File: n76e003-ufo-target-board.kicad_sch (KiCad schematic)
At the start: 12 parts, among them J1 CW308T_CONNBOARD, J4 Conn_01x02_Pin, U2 N76E003AT20

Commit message: Remove C2, add url to board
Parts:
- removed C2: 2.2uF, Capacitor_SMD:C_0805_2012Metric_Pad1.18x1.45mm_HandSolder, symbol Device:C_Small
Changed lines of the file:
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@@
   (junction (at 92.71 137.795) (diameter 0) (color 0 0 0 0)
   )
-  (junction (at 213.36 111.125) (diameter 0) (color 0 0 0 0)
-  )
   (junction (at 94.615 130.175) (diameter 0) (color 0 0 0 0)
   )
@@
   )
   (junction (at 193.04 117.475) (diameter 0) (color 0 0 0 0)
-  )
-  (junction (at 213.36 104.775) (diameter 0) (color 0 0 0 0)
   )
   (no_connect (at 121.285 155.575))
@@
   (no_connect (at 179.705 107.315))
   (no_connect (at 126.365 155.575))
+  (bus_entry (at -22.86 66.04) (size 2.54 2.54)
+    (stroke (width 0) (type default))
+  )
   (wire (pts (xy 53.34 108.585) (xy 53.34 117.475))
     (stroke (width 0) (type default))
@@
     (stroke (width 0) (type default))
   )
-  (wire (pts (xy 213.36 104.775) (xy 224.79 104.775))
-    (stroke (width 0) (type default))
-  )
   (wire (pts (xy 154.305 165.735) (xy 90.805 165.735))
     (stroke (width 0) (type default))
@@
     (stroke (width 0) (type default))
   )
-  (wire (pts (xy 224.79 111.125) (xy 224.79 109.855))
-    (stroke (width 0) (type default))
-  )
   (wire (pts (xy 78.74 137.795) (xy 92.71 137.795))
     (stroke (width 0) (type default))
@@
     (stroke (width 0) (type default))
   )
-  (wire (pts (xy 213.36 111.125) (xy 213.36 109.855))
+  (wire (pts (xy 213.36 109.855) (xy 213.36 113.03))
     (stroke (width 0) (type default))
   )
@@
     (stroke (width 0) (type default))
   )
-  (wire (pts (xy 213.36 113.03) (xy 213.36 111.125))
-    (stroke (width 0) (type default))
-  )
   (wire (pts (xy 154.305 155.575) (xy 154.305 165.735))
     (stroke (width 0) (type default))
@@
   )
   (wire (pts (xy 80.645 112.395) (xy 86.995 112.395))
-    (stroke (width 0) (type default))
-  )
-  (wire (pts (xy 213.36 111.125) (xy 224.79 111.125))
     (stroke (width 0) (type default))
   )
@@
         )
       )
-    )
-  )
-  (symbol (lib_id "Device:C_Small") (at 224.79 107.315 0) (unit 1)
-    (in_bom yes) (on_board yes) (dnp no) (fields_autoplaced)
-    (property "Reference" "C2" (at 227.33 106.6863 0)
-      (effects (font (size 1.27 1.27)) (justify left))
-    )
-    (property "Value" "2.2uF" (at 227.33 109.2263 0)
-      (effects (font (size 1.27 1.27)) (justify left))
-    )
-    (property "Footprint" "Capacitor_SMD:C_0805_2012Metric_Pad1.18x1.45mm_HandSolder" (at 224.79 107.315 0)
-      (effects (font (size 1.27 1.27)) hide)
-    )
-    (property "Datasheet" "~" (at 224.79 107.315 0)
-      (effects (font (size 1.27 1.27)) hide)
-    )
-    (pin "1")
-    (pin "2")
-    (instances
-      (project "n76e003-ufo-target-board"
-        (path "/e139b73c-4b3b-4226-b99b-9f4c47aa4c67"
-          (reference "C2") (unit 1)
-        )
-      )

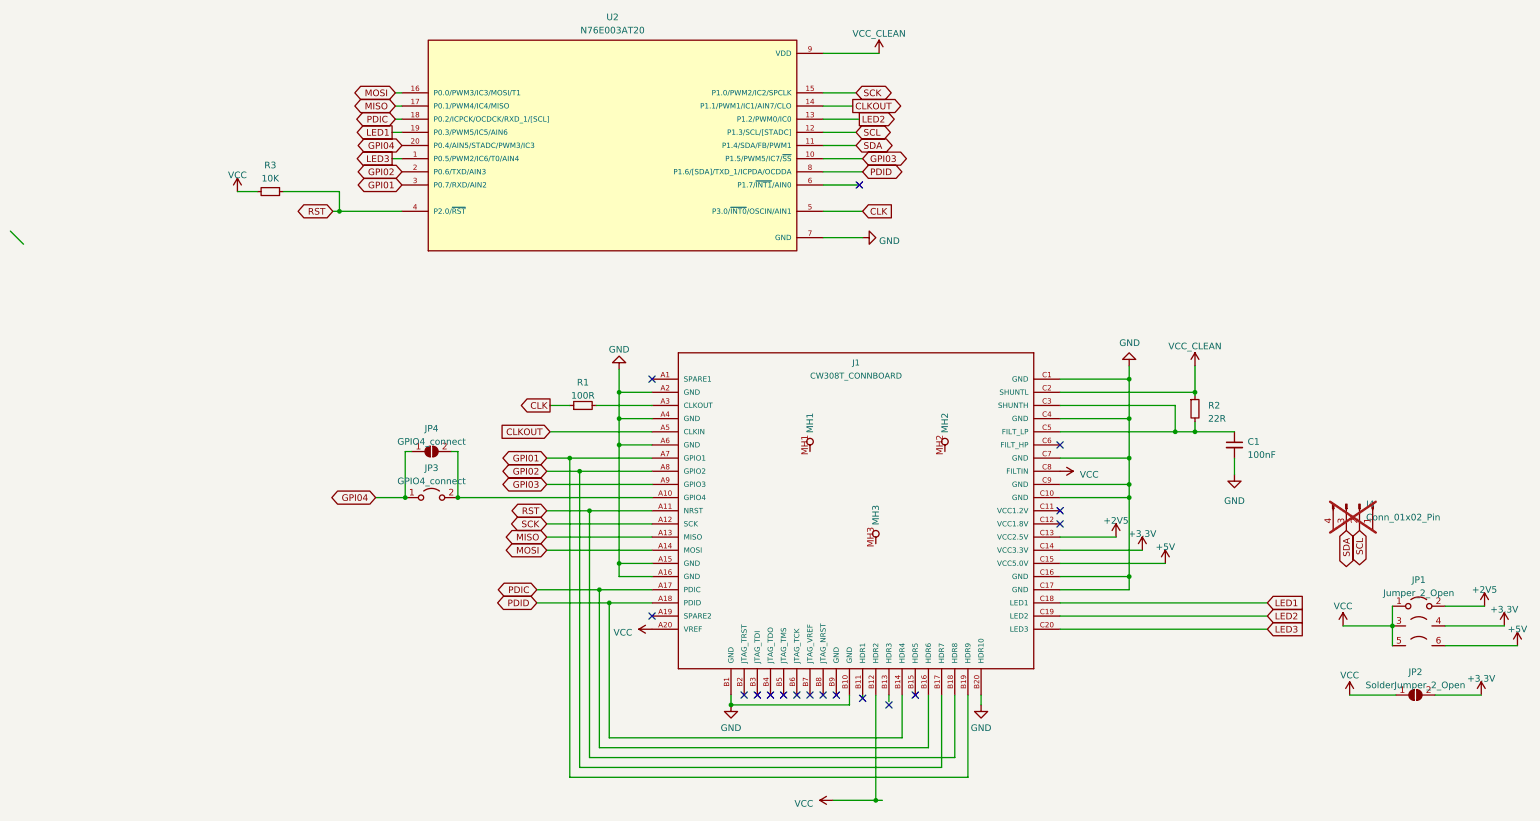
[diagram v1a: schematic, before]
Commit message: switch gpio1 and gpio2 lines, update gerbers, notes
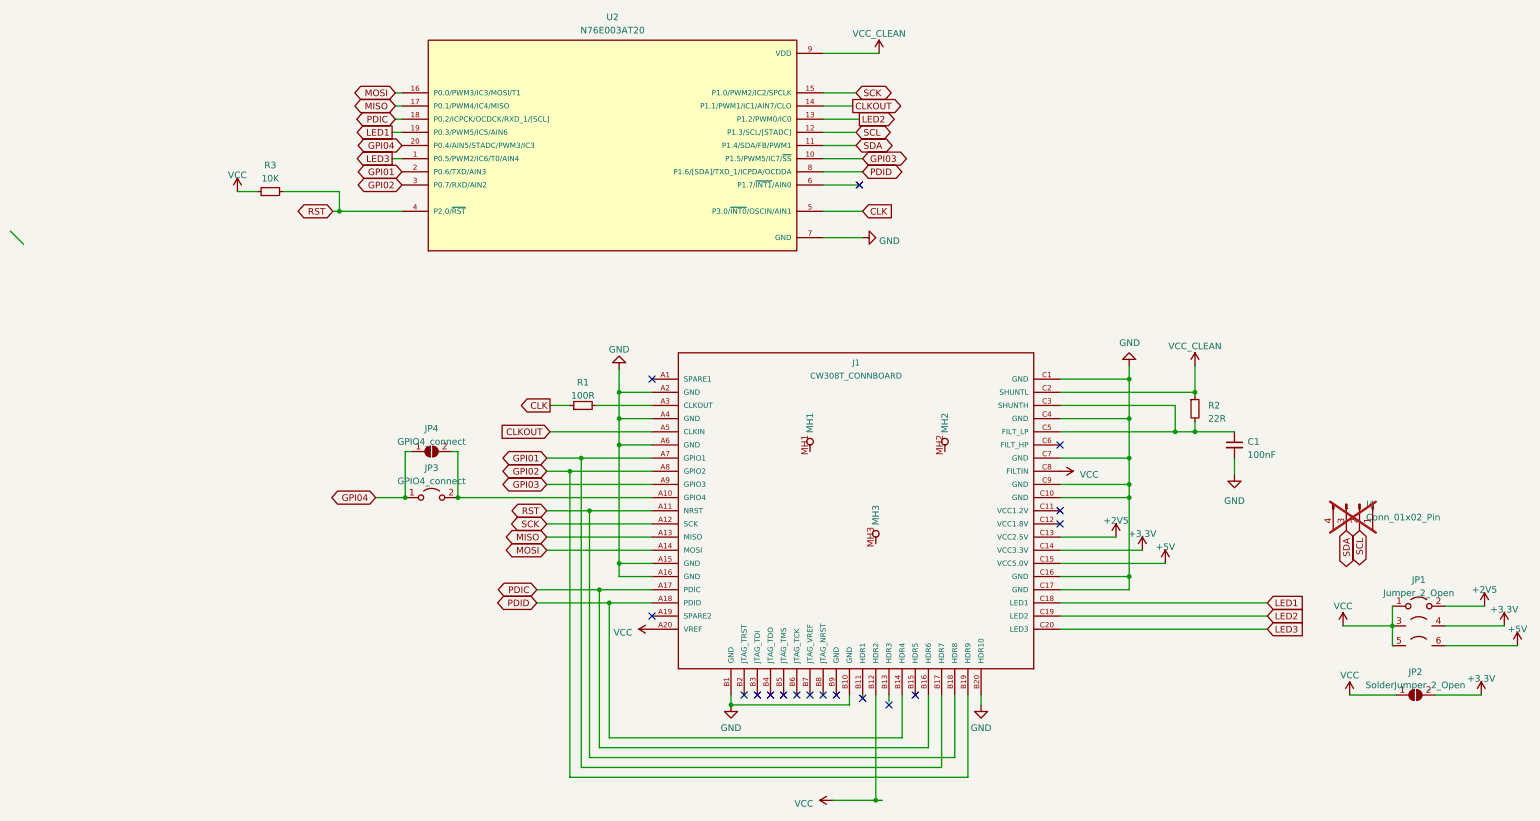
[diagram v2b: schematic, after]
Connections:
- net GPI01: now also J1.B17 (HDR7), U2.2 (P0.6/TXD/AIN3); no longer J1.B19 (HDR9), U2.3 (P0.7/RXD/AIN2)
- net GPI02: now also J1.B19 (HDR9), U2.3 (P0.7/RXD/AIN2); no longer J1.B17 (HDR7), U2.2 (P0.6/TXD/AIN3)
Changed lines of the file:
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@@
   (junction (at 205.74 97.155) (diameter 0) (color 0 0 0 0)
   )
-  (junction (at 86.995 112.395) (diameter 0) (color 0 0 0 0)
-  )
   (junction (at 243.84 142.24) (diameter 0) (color 0 0 0 0)
   )
@@
   (junction (at 116.205 157.48) (diameter 0) (color 0 0 0 0)
   )
-  (junction (at 85.09 109.855) (diameter 0) (color 0 0 0 0)
-  )
   (junction (at 88.9 120.015) (diameter 0) (color 0 0 0 0)
   )
@@
   (junction (at 201.93 104.775) (diameter 0) (color 0 0 0 0)
   )
+  (junction (at 85.1215 112.395) (diameter 0) (color 0 0 0 0)
+  )
   (junction (at 94.615 107.315) (diameter 0) (color 0 0 0 0)
+  )
+  (junction (at 87.3052 109.855) (diameter 0) (color 0 0 0 0)
   )
   (junction (at 53.34 117.475) (diameter 0) (color 0 0 0 0)
@@
     (stroke (width 0) (type default))
   )
-  (wire (pts (xy 86.995 169.545) (xy 86.995 112.395))
+  (wire (pts (xy 87.3052 169.5503) (xy 87.3052 109.855))
     (stroke (width 0) (type default))
   )
@@
     (stroke (width 0) (type default))
   )
-  (wire (pts (xy 85.09 109.855) (xy 100.965 109.855))
+  (wire (pts (xy 80.645 109.855) (xy 87.3052 109.855))
     (stroke (width 0) (type default))
   )
@@
     (stroke (width 0) (type default))
   )
-  (wire (pts (xy 85.09 171.45) (xy 85.09 109.855))
+  (wire (pts (xy 85.1215 171.45) (xy 85.1215 112.395))
     (stroke (width 0) (type default))
   )
@@
     (stroke (width 0) (type default))
   )
-  (wire (pts (xy 86.995 112.395) (xy 100.965 112.395))
+  (wire (pts (xy 85.1215 112.395) (xy 100.965 112.395))
     (stroke (width 0) (type default))
   )
@@
     (stroke (width 0) (type default))
   )
-  (wire (pts (xy 156.845 155.575) (xy 156.845 169.545))
+  (wire (pts (xy 87.3052 109.855) (xy 100.965 109.855))
+    (stroke (width 0) (type default))
+  )
+  (wire (pts (xy 156.845 155.575) (xy 156.845 169.5503))
     (stroke (width 0) (type default))
   )
@@
     (stroke (width 0) (type default))
   )
-  (wire (pts (xy 80.645 109.855) (xy 85.09 109.855))
-    (stroke (width 0) (type default))
-  )
   (wire (pts (xy 53.34 108.585) (xy 54.61 108.585))
     (stroke (width 0) (type default))
   )
-  (wire (pts (xy 80.645 112.395) (xy 86.995 112.395))
+  (wire (pts (xy 80.645 112.395) (xy 85.1215 112.395))
     (stroke (width 0) (type default))
   )
@@
     (stroke (width 0) (type default))
   )
-  (wire (pts (xy 156.845 169.545) (xy 86.995 169.545))
+  (wire (pts (xy 156.845 169.5503) (xy 87.3052 169.5503))
     (stroke (width 0) (type default))
   )
@@
     (stroke (width 0) (type default))
   )
-  (wire (pts (xy 161.925 171.45) (xy 85.09 171.45))
+  (wire (pts (xy 161.925 171.45) (xy 85.1215 171.45))
     (stroke (width 0) (type default))
   )
@@
     )
   )
+  (global_label "GPI01" (shape bidirectional) (at 52.705 54.61 180) (fields_autoplaced)
+    (effects (font (size 1.27 1.27)) (justify right))
+    (property "Intersheetrefs" "${INTERSHEET_REFS}" (at 43.1241 54.61 0)
+      (effects (font (size 1.27 1.27)) (justify right) hide)
+    )
+  )
   (global_label "CLKOUT" (shape output) (at 139.7 41.91 0) (fields_autoplaced)
     (effects (font (size 1.27 1.27)) (justify left))
@@
     )
   )
-  (global_label "GPI01" (shape bidirectional) (at 52.705 57.15 180) (fields_autoplaced)
+  (global_label "PDIC" (shape bidirectional) (at 78.74 135.255 180) (fields_autoplaced)
+    (effects (font (size 1.27 1.27)) (justify right))
+    (property "Intersheetrefs" "${INTERSHEET_REFS}" (at 70.3081 135.255 0)
+      (effects (font (size 1.27 1.27)) (justify right) hide)
+    )
+  )
+  (global_label "SDA" (shape bidirectional) (at 140.335 49.53 0) (fields_autoplaced)
+    (effects (font (size 1.27 1.27)) (justify left))
+    (property "Intersheetrefs" "${INTERSHEET_REFS}" (at 147.9202 49.53 0)
+      (effects (font (size 1.27 1.27)) (justify left) hide)
+    )
+  )
+  (global_label "SCL" (shape bidirectional) (at 237.49 123.825 270) (fields_autoplaced)
+    (effects (font (size 1.27 1.27)) (justify right))
+    (property "Intersheetrefs" "${INTERSHEET_REFS}" (at 237.49 131.3497 90)
+      (effects (font (size 1.27 1.27)) (justify right) hide)
+    )
+  )
+  (global_label "PDIC" (shape bidirectional) (at 51.435 44.45 180) (fields_autoplaced)
+    (effects (font (size 1.27 1.27)) (justify right))
+    (property "Intersheetrefs" "${INTERSHEET_REFS}" (at 43.0031 44.45 0)
+      (effects (font (size 1.27 1.27)) (justify right) hide)
+    )
+  )
+  (global_label "GPI04" (shape bidirectional) (at 47.625 117.475 180) (fields_autoplaced)
+    (effects (font (size 1.27 1.27)) (justify right))
+    (property "Intersheetrefs" "${INTERSHEET_REFS}" (at 38.0441 117.475 0)
+      (effects (font (size 1.27 1.27)) (justify right) hide)
+    )
+  )
+  (global_label "LED3" (shape output) (at 50.8 52.07 180) (fields_autoplaced)
+    (effects (font (size 1.27 1.27)) (justify right))
+    (property "Intersheetrefs" "${INTERSHEET_REFS}" (at 43.2376 52.07 0)
+      (effects (font (size 1.27 1.27)) (justify right) hide)
+    )
+  )
+  (global_label "MOSI" (shape bidirectional) (at 80.645 127.635 180) (fields_autoplaced)
+    (effects (font (size 1.27 1.27)) (justify right))
+    (property "Intersheetrefs" "${INTERSHEET_REFS}" (at 72.0317 127.635 0)
+      (effects (font (size 1.27 1.27)) (justify right) hide)
+    )
+  )
+  (global_label "RST" (shape bidirectional) (at 80.645 120.015 180) (fields_autoplaced)
+    (effects (font (size 1.27 1.27)) (justify right))
+    (property "Intersheetrefs" "${INTERSHEET_REFS}" (at 73.1808 120.015 0)
+      (effects (font (size 1.27 1.27)) (justify right) hide)
+    )
+  )
+  (global_label "GPI02" (shape bidirectional) (at 52.705 57.15 180) (fields_autoplaced)
     (effects (font (size 1.27 1.27)) (justify right))
     (property "Intersheetrefs" "${INTERSHEET_REFS}" (at 43.1241 57.15 0)
@@
     )
   )
-  (global_label "PDIC" (shape bidirectional) (at 78.74 135.255 180) (fields_autoplaced)
-    (effects (font (size 1.27 1.27)) (justify right))
-    (property "Intersheetrefs" "${INTERSHEET_REFS}" (at 70.3081 135.255 0)
-      (effects (font (size 1.27 1.27)) (justify right) hide)
-    )
-  )
-  (global_label "SDA" (shape bidirectional) (at 140.335 49.53 0) (fields_autoplaced)
-    (effects (font (size 1.27 1.27)) (justify left))
-    (property "Intersheetrefs" "${INTERSHEET_REFS}" (at 147.9202 49.53 0)
-      (effects (font (size 1.27 1.27)) (justify left) hide)
-    )
-  )
-  (global_label "SCL" (shape bidirectional) (at 237.49 123.825 270) (fields_autoplaced)
-    (effects (font (size 1.27 1.27)) (justify right))
-    (property "Intersheetrefs" "${INTERSHEET_REFS}" (at 237.49 131.3497 90)
-      (effects (font (size 1.27 1.27)) (justify right) hide)
-    )
-  )
-  (global_label "PDIC" (shape bidirectional) (at 51.435 44.45 180) (fields_autoplaced)
-    (effects (font (size 1.27 1.27)) (justify right))
-    (property "Intersheetrefs" "${INTERSHEET_REFS}" (at 43.0031 44.45 0)
-      (effects (font (size 1.27 1.27)) (justify right) hide)
-    )
-  )
-  (global_label "GPI04" (shape bidirectional) (at 47.625 117.475 180) (fields_autoplaced)
-    (effects (font (size 1.27 1.27)) (justify right))
-    (property "Intersheetrefs" "${INTERSHEET_REFS}" (at 38.0441 117.475 0)
-      (effects (font (size 1.27 1.27)) (justify right) hide)
-    )
-  )
-  (global_label "LED3" (shape output) (at 50.8 52.07 180) (fields_autoplaced)
-    (effects (font (size 1.27 1.27)) (justify right))
-    (property "Intersheetrefs" "${INTERSHEET_REFS}" (at 43.2376 52.07 0)
-      (effects (font (size 1.27 1.27)) (justify right) hide)
-    )
-  )
-  (global_label "MOSI" (shape bidirectional) (at 80.645 127.635 180) (fields_autoplaced)
-    (effects (font (size 1.27 1.27)) (justify right))
-    (property "Intersheetrefs" "${INTERSHEET_REFS}" (at 72.0317 127.635 0)
-      (effects (font (size 1.27 1.27)) (justify right) hide)
-    )
-  )
-  (global_label "RST" (shape bidirectional) (at 80.645 120.015 180) (fields_autoplaced)
-    (effects (font (size 1.27 1.27)) (justify right))
-    (property "Intersheetrefs" "${INTERSHEET_REFS}" (at 73.1808 120.015 0)
-      (effects (font (size 1.27 1.27)) (justify right) hide)
-    )
-  )
   (global_label "LED2" (shape input) (at 219.71 140.335 0) (fields_autoplaced)
     (effects (font (size 1.27 1.27)) (justify left))
@@
       (effects (font (size 1.27 1.27)) (justify right) hide)
     )
-  )
-  (global_label "GPI02" (shape bidirectional) (at 52.705 54.61 180) (fields_autoplaced)
-    (effects (font (size 1.27 1.27)) (justify right))
-    (property "Intersheetrefs" "${INTERSHEET_REFS}" (at 43.1241 54.61 0)
-      (effects (font (size 1.27 1.27)) (justify right) hide)
-    )

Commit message: add C2 footprint back, exclude from BOM by default
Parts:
- added C2: 2.2uF (OPT), Capacitor_SMD:C_0805_2012Metric_Pad1.18x1.45mm_HandSolder, symbol Device:C_Small
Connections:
- net GND: now also C2.2
- net at C1.1, J1.C3 (SHUNTH), J1.C5 (FILT_LP)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: now also C2.1
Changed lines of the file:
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@@
 (kicad_sch (version 20230121) (generator eeschema)
   (paper "A4")
+  (junction (at 213.36 104.775) (diameter 0) (color 0 0 0 0)
+  )
   (junction (at 63.5 117.475) (diameter 0) (color 0 0 0 0)
   )
@@
   )
   (junction (at 193.04 94.615) (diameter 0) (color 0 0 0 0)
+  )
+  (junction (at 213.36 111.1524) (diameter 0) (color 0 0 0 0)
   )
   (junction (at 116.205 157.48) (diameter 0) (color 0 0 0 0)
@@
     (stroke (width 0) (type default))
   )
+  (wire (pts (xy 213.36 104.775) (xy 224.7865 104.775))
+    (stroke (width 0) (type default))
+  )
   (wire (pts (xy 135.89 175.895) (xy 144.145 175.895))
     (stroke (width 0) (type default))
@@
     (stroke (width 0) (type default))
   )
+  (wire (pts (xy 213.36 111.1524) (xy 224.7865 111.1524))
+    (stroke (width 0) (type default))
+  )
   (wire (pts (xy 146.685 156.845) (xy 146.685 155.575))
     (stroke (width 0) (type default))
@@
     (stroke (width 0) (type default))
   )
+  (wire (pts (xy 224.7865 104.775) (xy 224.7865 104.8024))
+    (stroke (width 0) (type default))
+  )
+  (wire (pts (xy 213.36 109.855) (xy 213.36 111.1524))
+    (stroke (width 0) (type default))
+  )
   (wire (pts (xy 78.74 137.795) (xy 92.71 137.795))
     (stroke (width 0) (type default))
@@
     (stroke (width 0) (type default))
   )
-  (wire (pts (xy 213.36 109.855) (xy 213.36 113.03))
+  (wire (pts (xy 213.3565 111.1524) (xy 213.36 111.1524))
     (stroke (width 0) (type default))
   )
@@
     (stroke (width 0) (type default))
   )
+  (wire (pts (xy 213.36 111.1524) (xy 213.36 113.03))
+    (stroke (width 0) (type default))
+  )
   (wire (pts (xy 193.04 94.615) (xy 193.04 102.235))
     (stroke (width 0) (type default))
@@
   )
   (wire (pts (xy 90.17 99.695) (xy 100.965 99.695))
+    (stroke (width 0) (type default))
+  )
+  (wire (pts (xy 224.7865 111.1524) (xy 224.7865 109.8824))
     (stroke (width 0) (type default))
   )
@@
         )
       )
+    )
+  )
+  (symbol (lib_id "Device:C_Small") (at 224.7865 107.3424 0) (unit 1)
+    (in_bom no) (on_board yes) (dnp no) (fields_autoplaced)
+    (property "Reference" "C2" (at 227.33 106.0787 0)
+      (effects (font (size 1.27 1.27)) (justify left))
+    )
+    (property "Value" "2.2uF (OPT)" (at 227.33 108.6187 0)
+      (effects (font (size 1.27 1.27)) (justify left))
+    )
+    (property "Footprint" "Capacitor_SMD:C_0805_2012Metric_Pad1.18x1.45mm_HandSolder" (at 224.7865 107.3424 0)
+      (effects (font (size 1.27 1.27)) hide)
+    )
+    (property "Datasheet" "~" (at 224.7865 107.3424 0)
+      (effects (font (size 1.27 1.27)) hide)
+    )
+    (pin "1")
+    (pin "2")
+    (instances
+      (project "n76e003-ufo-target-board"
+        (path "/e139b73c-4b3b-4226-b99b-9f4c47aa4c67"
+          (reference "C2") (unit 1)
+        )
+      )

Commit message: v1.3
Remove GPIO4 connect header, bump shunt resistor value to 51R, update on-board notes
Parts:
- removed JP3: GPIO4_connect, Connector_PinHeader_2.54mm:PinHeader_1x02_P2.54mm_Vertical, symbol Jumper:Jumper_2_Open
- removed JP4: GPIO4_connect, Jumper:SolderJumper-2_P1.3mm_Open_RoundedPad1.0x1.5mm, symbol Jumper:SolderJumper_2_Open
- added C3: 10uF, Capacitor_SMD:C_0805_2012Metric_Pad1.18x1.45mm_HandSolder, symbol Device:C_Small
- R2: value 22R -> 51R
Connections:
- net GND: now also C3.2
- net GPI04: now also J1.A10 (GPIO4)
- net RST: now also R3.2, C3.1; no longer R3.1
- net VCC: now also R3.1; no longer R3.2
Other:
- moved on the sheet: R3
